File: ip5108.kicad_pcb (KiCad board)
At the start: 2 copper layers, 66.7 x 33 mm, 31 parts, among them IC1 IP5108, IC2 SY8008B, J1 DB9_Female, J2 Conn_01x02, U1 STEPDOWN12_5

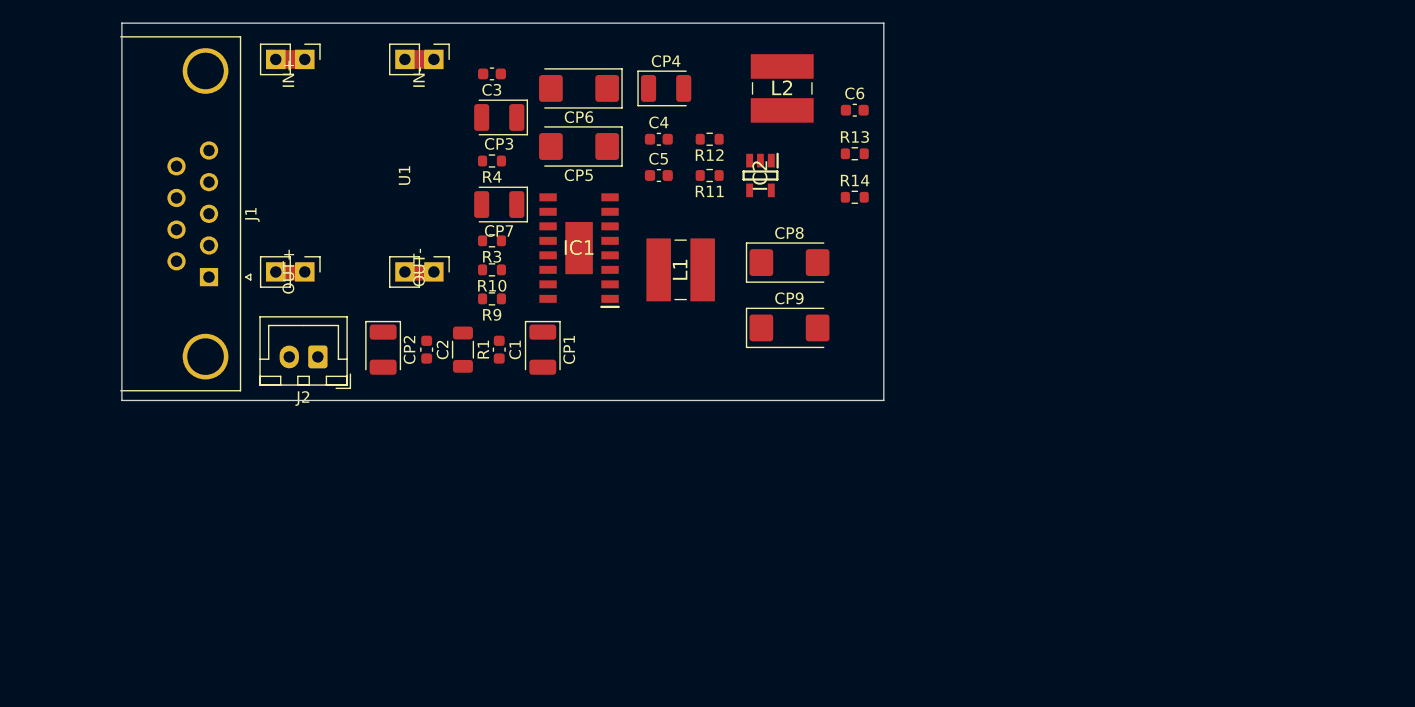
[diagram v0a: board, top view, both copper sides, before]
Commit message: IP5108 in Unterschaltplan verschoben
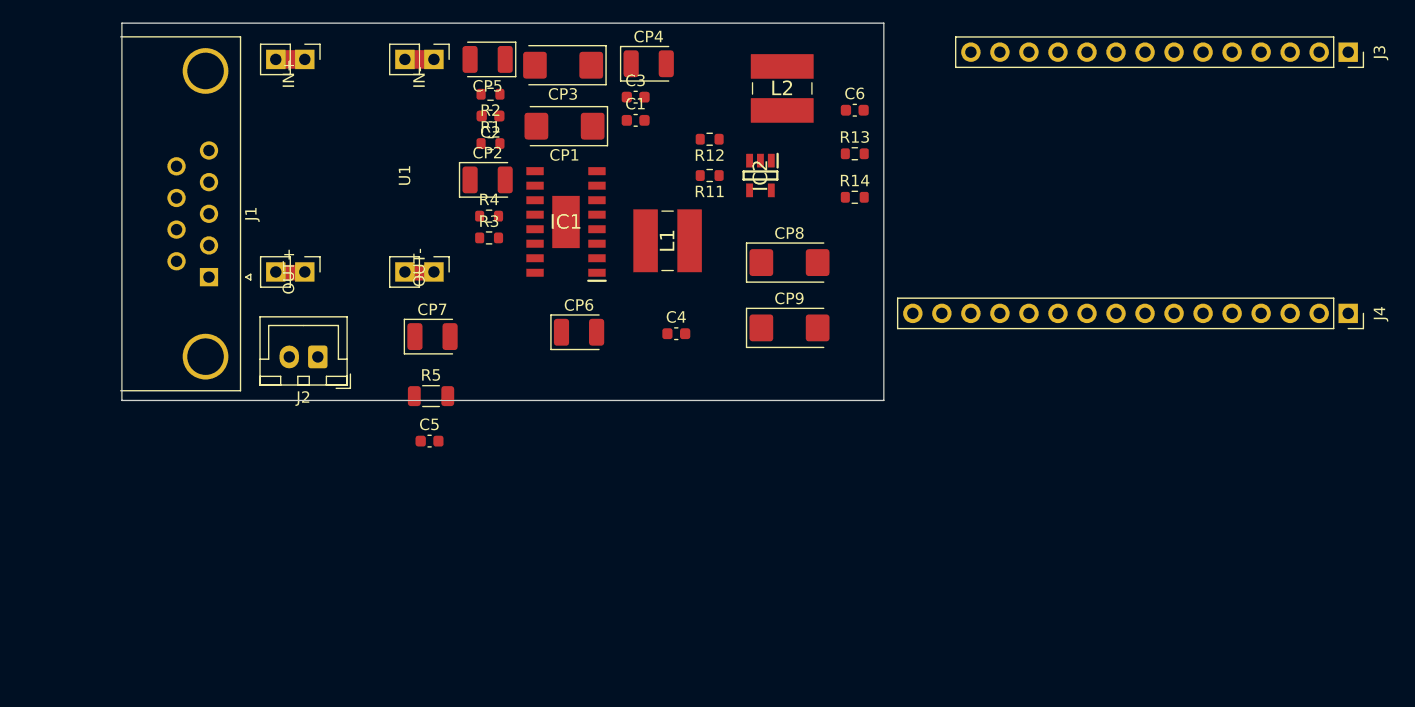
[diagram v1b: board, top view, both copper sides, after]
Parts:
- removed R10, R9: 3.3k, Resistor_SMD:R_0603_1608Metric
- added J3: Conn_01x14, Connector_PinSocket_2.54mm:PinSocket_1x14_P2.54mm_Vertical, F.Cu at (215.9, 78.7)
- added J4: Conn_01x16, Connector_PinSocket_2.54mm:PinSocket_1x16_P2.54mm_Vertical, F.Cu at (215.9, 101.6)
- added R2: 1K, Resistor_SMD:R_0603_1608Metric, F.Cu at (140.8, 82.4)
- added R5: 10mOhm, Resistor_SMD:R_1206_3216Metric, F.Cu at (135.6, 108.8)
- C3: value 104 -> 4.7nF
- C5: value 4.7nF -> 104
- CP1, CP3: value 10uF -> 22uF; footprint Capacitor_Tantalum_SMD:CP_EIA-3528-21_Kemet-B -> Capacitor_Tantalum_SMD:CP_EIA-6032-28_Kemet-C
- CP5, CP6: value 22uF -> 10uF; footprint Capacitor_Tantalum_SMD:CP_EIA-6032-28_Kemet-C -> Capacitor_Tantalum_SMD:CP_EIA-3528-21_Kemet-B
- R1: value 10mOhm -> 2R; footprint Resistor_SMD:R_1206_3216Metric -> Resistor_SMD:R_0603_1608Metric
- R3: value 2R -> 3.3k
- R4: value 1K -> 3.3k
- moved C5 30.7 mm to (135.5, 112.8)
- moved C1 23.3 mm to (153.5, 84.7), turned to 0 degrees
- moved CP6 21.3 mm to (148.6, 103.3), turned to 0 degrees
- moved C2 21.2 mm to (140.8, 84.3), turned to 180 degrees
- moved CP1 19.7 mm to (147.3, 85.2), turned to 180 degrees
- moved R1 18.2 mm to (140.8, 86.7), turned to 0 degrees
- moved CP2 17.4 mm to (140.6, 89.9), turned to 0 degrees
- moved C4 17.1 mm to (157.1, 103.4)
- moved CP7 12.9 mm to (135.8, 103.6), turned to 0 degrees
- moved C3 12.7 mm to (153.5, 82.7), turned to 0 degrees
- moved CP5 11.0 mm to (140.6, 79.4)
- moved CP3 7.22 mm to (147.2, 79.9)
- moved R4 4.83 mm to (140.7, 93.1), turned to 0 degrees
- moved L1 2.79 mm to (156.3, 95.2)
- moved CP4 2.64 mm to (154.7, 79.8)
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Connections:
- C1 pad 1: +BATT -> 5VOUT
- C2 pad 1: Net-(C2-Pad1) -> 5VIN
- C2 pad 2: GND -> Net-(C2-Pad2)
- C3 pad 1: VIN -> 5VOUT
- C4 pad 1: 5VOUT -> Net-(C4-Pad1)
- C5 pad 1: 5VOUT -> +BATT
- C5 pad 2: Net-(C5-Pad2) -> GND
- CP1 pad 1: +BATT -> 5VOUT
- CP2 pad 1: Net-(C2-Pad1) -> Net-(CP2-Pad1)
- CP3 pad 1: VIN -> 5VOUT
- CP3 pad 2: Net-(C3-Pad2) -> GND
- CP5 pad 1: 5VOUT -> 5VIN
- CP5 pad 2: GND -> Net-(C2-Pad2)
- CP6 pad 1: 5VOUT -> Net-(C4-Pad1)
- CP7 pad 1: Net-(CP7-Pad1) -> +BATT
- IC1 pad 1: Net-(C2-Pad1) -> Net-(C4-Pad1)
- IC1 pad 3: Net-(C5-Pad2) -> Net-(C3-Pad2)
- IC1 pad 4: Net-(C5-Pad2) -> Net-(C3-Pad2)
- IC1 pad 7: VIN -> 5VIN
- L1 pad 1: Net-(C2-Pad1) -> Net-(C4-Pad1)
- L1 pad 2: Net-(C5-Pad2) -> Net-(C3-Pad2)
- R1 pad 1: +BATT -> Net-(CP2-Pad1)
- R1 pad 2: Net-(C2-Pad1) -> 5VIN
- R3 pad 1: Net-(CP7-Pad1) -> Net-(IC1-Pad12)
- R3 pad 2: VIN -> SDA
- R4 pad 1: VIN -> Net-(IC1-Pad12)
- R4 pad 2: Net-(C3-Pad2) -> SCL
- U1 pad 5: VIN -> 5VIN
- U1 pad 6: VIN -> 5VIN

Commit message: IP5108 in Unterverzeichnis verschoben
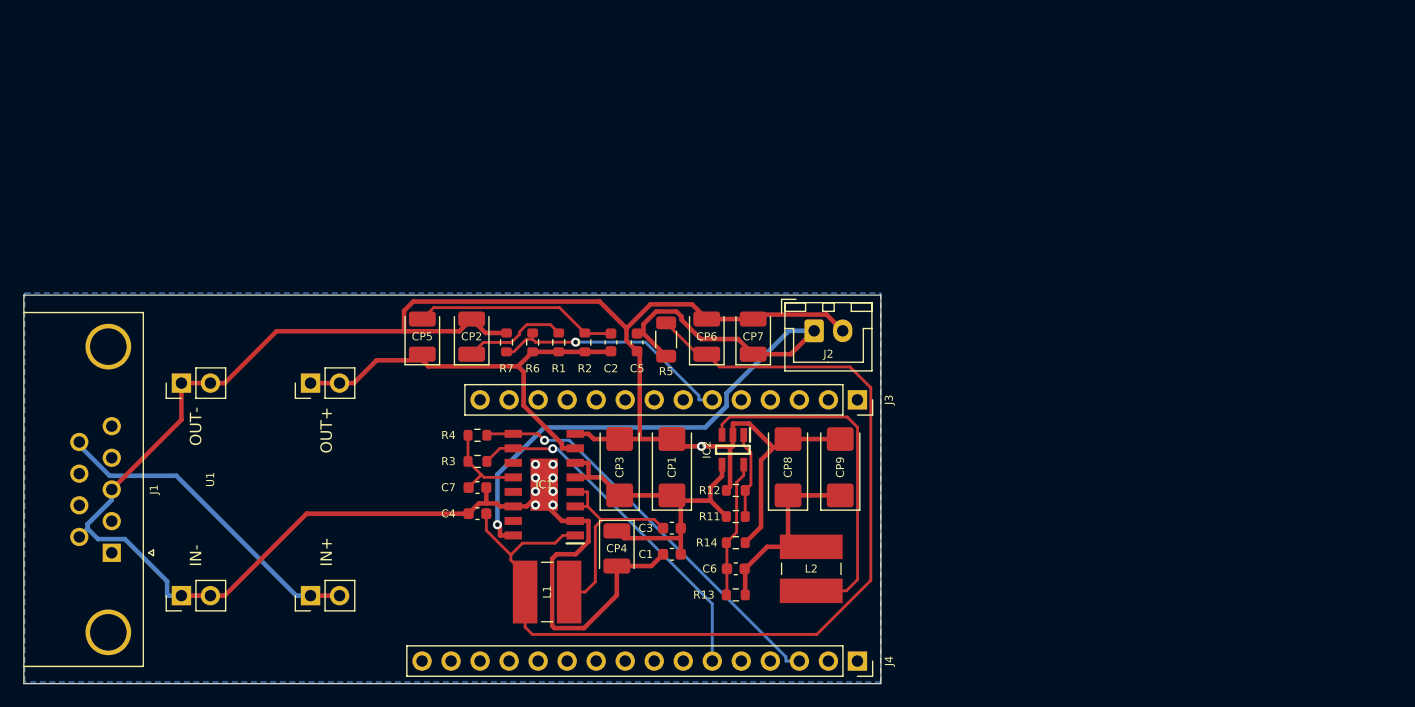
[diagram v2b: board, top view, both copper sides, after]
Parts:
- added C7: 2.2uF, Capacitor_SMD:C_0603_1608Metric, F.Cu at (139.7, 116.8)
- added R6: R, Resistor_SMD:R_0603_1608Metric, F.Cu at (144.5, 104.1)
- added R7: R, Resistor_SMD:R_0603_1608Metric, F.Cu at (142.2, 104.1)
- IC1: footprint SamacSys_Parts:SOIC127P600X175-17N -> IP5108:IP5108
- L1, L2: footprint SamacSys_Parts:CD54NP470LC -> IP5108:CD54_Inductor
- U1: footprint ip5108:StepDownBreakout -> StepDownBreakout:StepDownBreakout
- moved J4 52.6 mm to (172.9, 132.0)
- moved J3 52.6 mm to (172.9, 109.2)
- moved J2 43.5 mm to (169.2, 103.1), turned to 0 degrees
- moved CP4 42.5 mm to (151.9, 122.2), turned to 270 degrees
- moved L2 42.1 mm to (168.9, 124.0)
- moved C6 41.5 mm to (162.3, 124.0), turned to 180 degrees
- moved R13 40.0 mm to (162.3, 126.2), turned to 180 degrees
- moved C1 38.1 mm to (156.7, 122.7), turned to 180 degrees
- moved C3 37.9 mm to (156.7, 120.4), turned to 180 degrees
- moved CP3 35.5 mm to (152.1, 115.1), turned to 90 degrees
- moved L1 32.5 mm to (145.8, 126.0), turned to 90 degrees
- moved R14 32.0 mm to (162.3, 121.7)
- moved CP1 31.3 mm to (156.7, 115.1), turned to 90 degrees
- moved R12 30.8 mm to (162.3, 117.1)
- moved R11 29.9 mm to (162.3, 119.4), turned to 0 degrees
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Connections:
- net Net-(J3-Pad11) renamed INT
- J3 pad 6: Net-(J3-Pad6) -> EXTPOW
- J4 pad 3: Net-(J4-Pad3) -> SCL
- J4 pad 6: Net-(J4-Pad6) -> SDA
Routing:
- net GND: track 0.00 -> 222.2 mm, vias 0 -> 9
- net Net-(C4-Pad1): track 0.00 -> 87.3 mm
- net +BATT: track 0.00 -> 62.3 mm, vias 0 -> 1
- net 5VIN: track 0.00 -> 38.3 mm
- net SCL: track 0.00 -> 35.8 mm, vias 0 -> 1
- net Net-(IC2-Pad3): track 0.00 -> 31.2 mm
- net 5VOUT: track 0.00 -> 31.2 mm
- net SDA: track 0.00 -> 30.8 mm, vias 0 -> 1
- net +12V: track 0.00 -> 28.5 mm
- net EXTPOW: track 0.00 -> 21.4 mm, vias 0 -> 1
- net Net-(C3-Pad2): track 0.00 -> 19.2 mm
- net +3V3: track 0.00 -> 18.0 mm
- net Net-(C2-Pad2): track 0.00 -> 17.9 mm
- net Net-(C6-Pad2): track 0.00 -> 12.1 mm
- net Net-(CP2-Pad1): track 0.00 -> 9.11 mm
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- added copper zone on B.Cu, net GND
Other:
- board size 66.7 x 33 mm -> 75 x 34 mm
- net class Dick added: clearance 0.2, trace_width 0.4, via_dia 0.8, via_drill 0.4
